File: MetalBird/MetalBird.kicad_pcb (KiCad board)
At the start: 2 copper layers, 36 x 36 mm, 63 parts, among them J1 Battery Conn, J10 VTX Conn, J2 SWD, J3 ESC1, J4 ESC2, J5 ESC3, J6 ESC4, J7 ELRS Reciver, J8 USB/UART DEBUG, J9 Camera Conn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

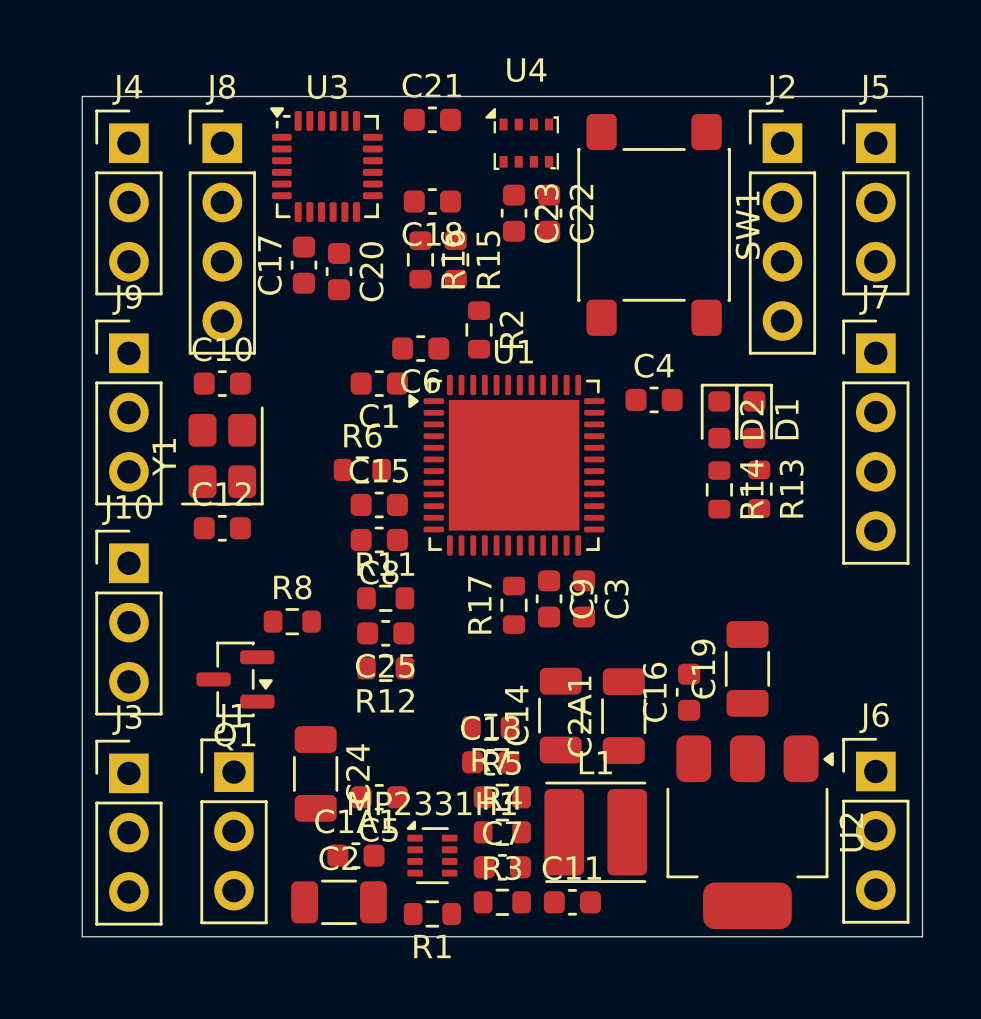
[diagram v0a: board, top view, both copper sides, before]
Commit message: Routing Complete
- yet to fix cosmetic stuff (silk overlap)
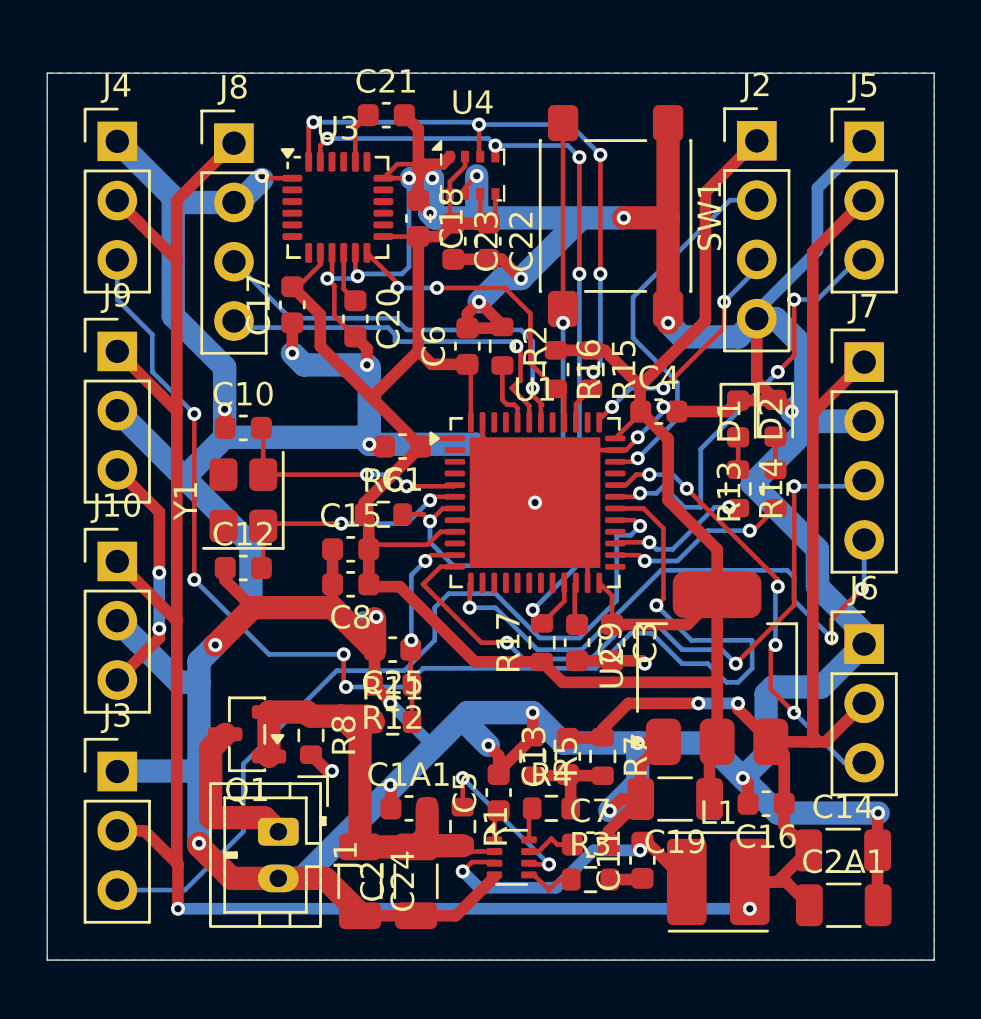
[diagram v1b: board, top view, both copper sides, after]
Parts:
- J1: footprint Connector_PinHeader_2.54mm:PinHeader_1x03_P2.54mm_Vertical -> Connector_JST:JST_PH_B2B-PH-K_1x02_P2.00mm_Vertical
- moved C14 13.4 mm to (133.1, 82.3), turned to 0 degrees
- moved C2A1 12.4 mm to (133.1, 84.7), turned to 0 degrees
- moved R16 7.47 mm to (120.8, 61.7)
- moved R15 7.47 mm to (122.3, 61.7)
- moved U2 7.14 mm to (127.7, 74.5), turned to 90 degrees
- moved C19 6.38 mm to (125.9, 80.1), turned to 180 degrees
- moved C16 5.80 mm to (129.8, 80.3), turned to 180 degrees
- moved L1 5.66 mm to (127.8, 83.7)
- moved J6 5.48 mm to (134.0, 73.5)
- moved R11 5.31 mm to (113.8, 76.8)
- moved C5 5.12 mm to (118.3, 79.8), turned to 90 degrees
- moved C24 4.98 mm to (112.4, 83.6)
- moved R7 4.96 mm to (122.8, 78.3), turned to -90 degrees
- moved R8 4.94 mm to (110.3, 77.4), turned to -90 degrees
- moved R1 3.97 mm to (116.8, 81.3), turned to -90 degrees
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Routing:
- net GND: track 0.00 -> 307.8 mm, vias 0 -> 32
- net 5V: track 0.00 -> 127.1 mm, vias 0 -> 4
- net 3.3V: track 0.00 -> 108.4 mm
- net Net-(J4-Pin_3): track 0.00 -> 55.6 mm, vias 0 -> 5
- net SCL: track 0.00 -> 35.8 mm, vias 0 -> 5
- net Net-(J3-Pin_3): track 0.00 -> 35.8 mm, vias 0 -> 1
- net USART2_TX: track 0.00 -> 29.5 mm, vias 0 -> 3
- net Net-(SW1-B): track 0.00 -> 28.2 mm, vias 0 -> 2
- net SDA: track 0.00 -> 28.0 mm, vias 0 -> 5
- net USART2_RX: track 0.00 -> 25.3 mm, vias 0 -> 3
- net 7.4V: track 0.00 -> 20.2 mm
- net Net-(J6-Pin_3): track 0.00 -> 19.1 mm, vias 0 -> 5
- net Net-(J5-Pin_3): track 0.00 -> 18.5 mm, vias 0 -> 3
- net USART1_TX: track 0.00 -> 17.9 mm, vias 0 -> 1
- net USART1_RX: track 0.00 -> 16.6 mm, vias 0 -> 1
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- added copper zone on B.Cu, net GND
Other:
- board size 36 x 36 mm -> 38 x 38 mm

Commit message: Gerber files and components list
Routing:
- net Net-(J4-Pin_3): track 55.6 -> 54.2 mm
- net GND: track 307.8 -> 307.2 mm
